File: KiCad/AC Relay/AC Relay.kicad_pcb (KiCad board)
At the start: 2 copper layers, 49.5 x 49.5 mm, 17 parts, among them J1 Screw_Terminal_01x02, J2 Conn_01x06_Female, J3 Screw_Terminal_01x02, K1 1461492-2, Q1 FDN537N, SW1 SW_Push, U1 BU33SD5WG-TR, U2 ESP-12E, U3 HLK-PM01

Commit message: title edited
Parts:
- added REF**: TerminalBlock_RND_205-00045_1x02_P5.00mm_Horizontal, TerminalBlock_RND:TerminalBlock_RND_205-00045_1x02_P5.00mm_Horizontal, F.Cu at (59.7, 61.0)
- moved J3 0.82 mm to (75.3, 71.0)
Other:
- board text added: "BTBM_1 Rev.: 1 S/N:0001"
- board text added: "DANGER KEEP OUT HIGH VOLTAGE AREA"
- board text added: "Relay 10A"
- board text removed: "AC Relay - ESP8266 Design by Enrique Gómez CC BY-SA 4.0 enriquegomez.me Rev.: 4 - S/N:"
- board text removed: "DANGER HIGH VOLTAGE AREA"
- board text removed: "Relay Max. 16 A"

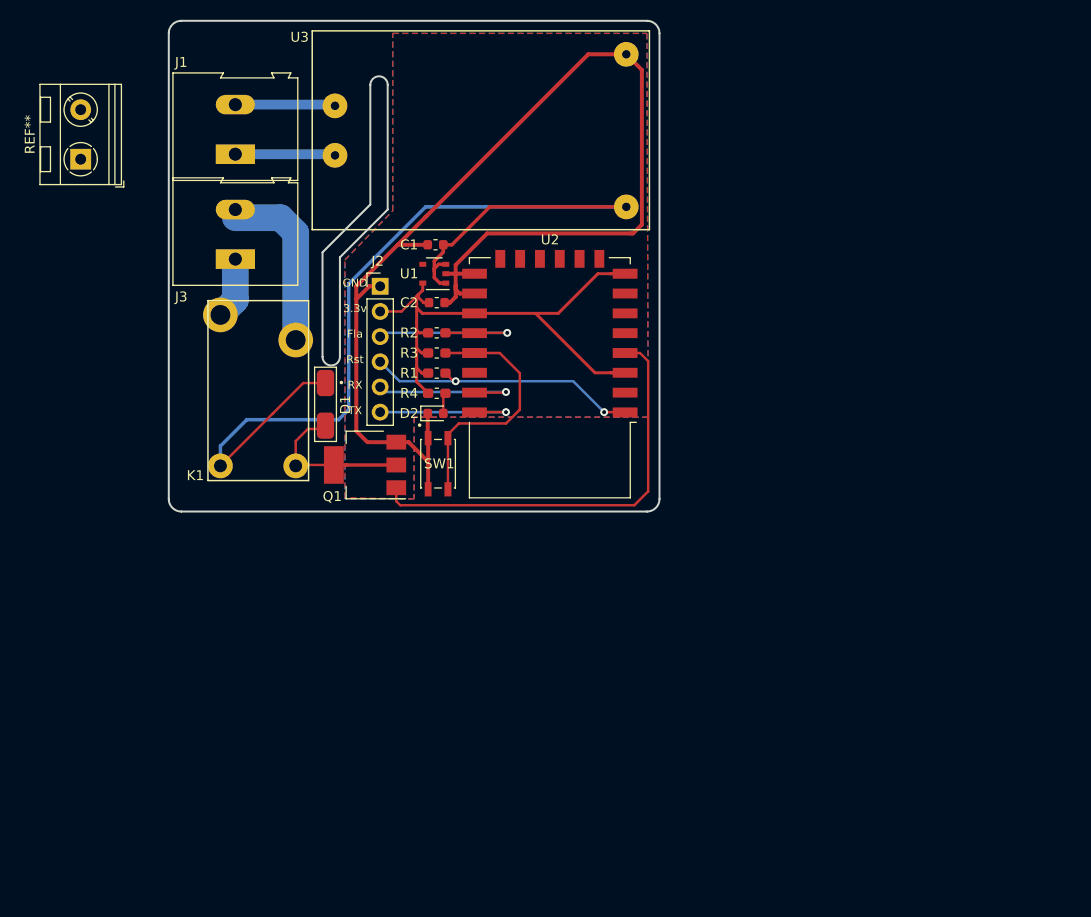
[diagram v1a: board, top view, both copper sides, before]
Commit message: until components placemaent
done all until com placement, but had isssue in edge cut .
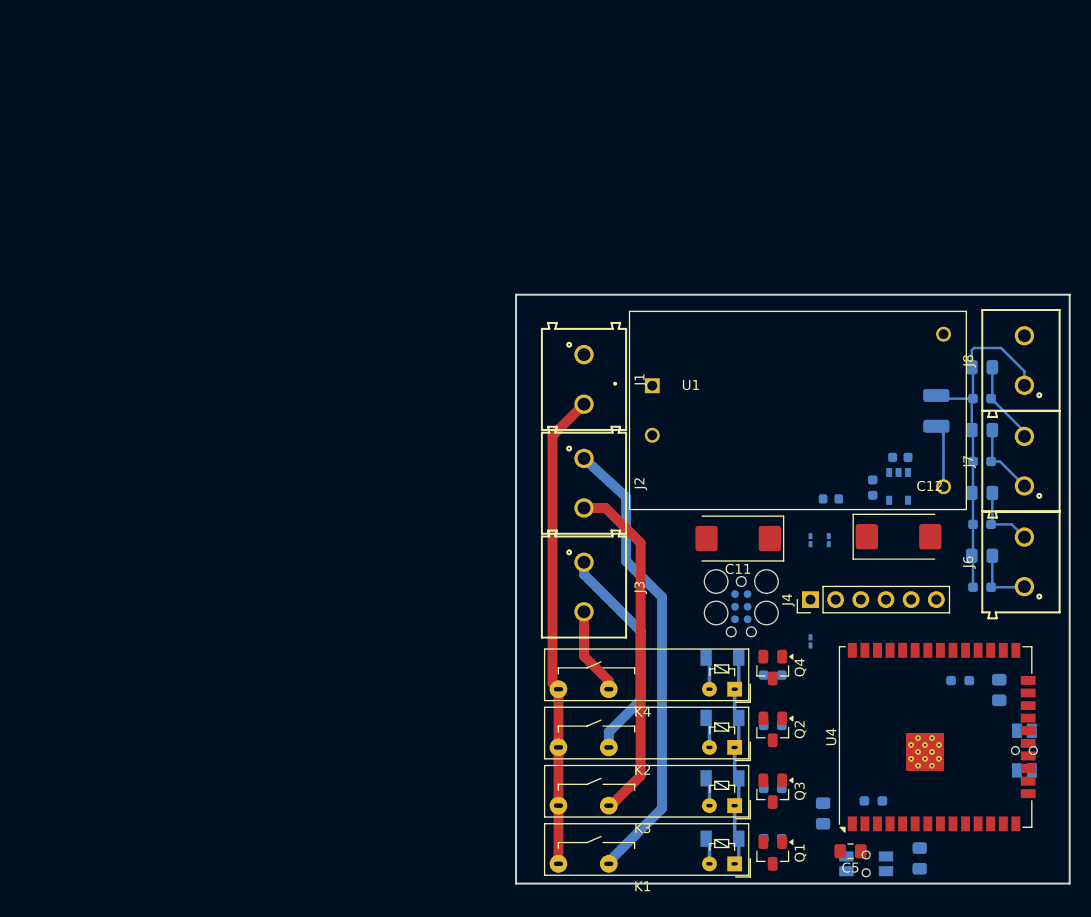
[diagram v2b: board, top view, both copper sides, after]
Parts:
- removed R1, R2, R3: 10k, Resistor_SMD:R_0603_1608Metric_Pad1.05x0.95mm_HandSolder
- removed R4: 82.5, Resistor_SMD:R_0603_1608Metric_Pad1.05x0.95mm_HandSolder
- removed REF**: TerminalBlock_RND_205-00045_1x02_P5.00mm_Horizontal, TerminalBlock_RND:TerminalBlock_RND_205-00045_1x02_P5.00mm_Horizontal
- removed SW1: SW_Push, Button_Switch_SMD:SW_SPST_EVQP2
- removed U3: HLK-PM01, red:HLK-PM01
- added C10: 0.1uf, Capacitor_SMD:C_0805_2012Metric_Pad1.18x1.45mm_HandSolder, B.Cu at (150.7, 88.3)
- added C11: 100uF T cap, Capacitor_Tantalum_SMD:CP_EIA-7343-20_Kemet-V_Pad2.25x2.55mm_HandSolder, F.Cu at (126.1, 99.2)
- added C12: 100uF T cap, Capacitor_Tantalum_SMD:CP_EIA-7343-20_Kemet-V_Pad2.25x2.55mm_HandSolder, F.Cu at (142.2, 99.1)
- added C3: 0.1uf, Capacitor_SMD:C_0805_2012Metric_Pad1.18x1.45mm_HandSolder, B.Cu at (144.4, 131.5)
- added C4: 10uf, Capacitor_SMD:C_0805_2012Metric_Pad1.18x1.45mm_HandSolder, B.Cu at (134.6, 127.0)
- added C5: 0.1uf, Capacitor_SMD:C_0805_2012Metric_Pad1.18x1.45mm_HandSolder, F.Cu at (137.4, 130.8)
- added C6: 0.1uf, Capacitor_SMD:C_0805_2012Metric_Pad1.18x1.45mm_HandSolder, B.Cu at (152.4, 114.5)
- added C7: 0.1uf, Capacitor_SMD:C_0805_2012Metric_Pad1.18x1.45mm_HandSolder, B.Cu at (150.7, 94.6)
- added C8: 0.1uf, Capacitor_SMD:C_0805_2012Metric_Pad1.18x1.45mm_HandSolder, B.Cu at (150.7, 101.0)
- added C9: 0.1uf, Capacitor_SMD:C_0805_2012Metric_Pad1.18x1.45mm_HandSolder, B.Cu at (150.7, 82.0)
- added D3: LL4148, Rak_FP_Library:LL4148, B.Cu at (124.5, 117.3)
- added D4: LL4148, Rak_FP_Library:LL4148, B.Cu at (124.5, 123.4)
- added D5: LL4148, Rak_FP_Library:LL4148, B.Cu at (124.5, 111.3)
- added J4: Conn_01x06_Female, Connector_PinHeader_2.54mm:PinHeader_1x06_P2.54mm_Vertical, F.Cu at (133.3, 105.4)
- added J6: TB002-500-02BE, Rak_FP_Library:2_terminal_block_small, F.Cu at (154.9, 101.6)
- added J7: TB002-500-02BE, Rak_FP_Library:2_terminal_block_small, F.Cu at (154.9, 91.4)
- added J8: TB002-500-02BE, Rak_FP_Library:2_terminal_block_small, F.Cu at (154.9, 81.3)
- added J9: Conn_ARM_SWD_TagConnect_TC2030, Connector:Tag-Connect_TC2030-IDC-FP_2x03_P1.27mm_Vertical, B.Cu at (126.4, 106.1)
- added K2: 1-2071556-1, Rak_FP_Library:Relay_SPST_Fanahar_5A, F.Cu at (125.7, 120.3)
- added K3: 1-2071556-1, Rak_FP_Library:Relay_SPST_Fanahar_5A, F.Cu at (125.7, 126.2)
- added K4: 1-2071556-1, Rak_FP_Library:Relay_SPST_Fanahar_5A, F.Cu at (125.7, 114.5)
- added Q2: FDN537N, Package_TO_SOT_SMD:SuperSOT-3, F.Cu at (129.5, 118.5)
- added Q3: FDN537N, Package_TO_SOT_SMD:SuperSOT-3, F.Cu at (129.5, 124.7)
- added Q4: FDN537N, Package_TO_SOT_SMD:SuperSOT-3, F.Cu at (129.5, 112.3)
- added R10: 10K, Resistor_SMD:R_0603_1608Metric_Pad0.98x0.95mm_HandSolder, B.Cu at (150.7, 91.5)
- added R11: 330R, Resistor_SMD:R_1210_3225Metric_Pad1.30x2.65mm_HandSolder, B.Cu at (146.1, 86.4)
- added R12: 1K, Resistor_SMD:R_0603_1608Metric_Pad0.98x0.95mm_HandSolder, B.Cu at (129.5, 129.5)
- added R13: 0R, Resistor_SMD:R_0201_0603Metric_Pad0.64x0.40mm_HandSolder, B.Cu at (133.3, 109.6)
- added R14: 0R, Resistor_SMD:R_0201_0603Metric_Pad0.64x0.40mm_HandSolder, B.Cu at (133.3, 99.4)
- added R15: NA, Resistor_SMD:R_0201_0603Metric_Pad0.64x0.40mm_HandSolder, B.Cu at (135.2, 99.4)
- added R16: 1K, Resistor_SMD:R_0603_1608Metric_Pad0.98x0.95mm_HandSolder, B.Cu at (129.5, 113.0)
- added R17: 1K, Resistor_SMD:R_0603_1608Metric_Pad0.98x0.95mm_HandSolder, B.Cu at (129.5, 124.5)
- added R18: 1K, Resistor_SMD:R_0603_1608Metric_Pad0.98x0.95mm_HandSolder, B.Cu at (129.5, 118.1)
- added R5: 10K, Resistor_SMD:R_0603_1608Metric_Pad0.98x0.95mm_HandSolder, B.Cu at (148.5, 113.6)
- added R6: 12K, Resistor_SMD:R_0603_1608Metric_Pad0.98x0.95mm_HandSolder, B.Cu at (139.7, 125.7)
- added R7: 10K, Resistor_SMD:R_0603_1608Metric_Pad0.98x0.95mm_HandSolder, B.Cu at (150.7, 97.8)
- added R8: 10K, Resistor_SMD:R_0603_1608Metric_Pad0.98x0.95mm_HandSolder, B.Cu at (150.7, 104.2)
- added R9: 10K, Resistor_SMD:R_0603_1608Metric_Pad0.98x0.95mm_HandSolder, B.Cu at (150.7, 85.1)
- added SW2: Boot, Rak_FP_Library:SW_SPST_withpost, B.Cu at (154.9, 120.7)
- added SW3: Rst, Rak_FP_Library:SW_SPST_withpost, B.Cu at (139.0, 132.1)
- added U4: ESP32-WROOM-32UE, Rak_FP_Library:ESP32-WROOM-32UE, F.Cu at (146.0, 119.3)
- C1, C2: value 0.47uF -> 1uF; moved to B.Cu
- D1: value RGF1B -> LED_verde; footprint Diode_SMD:D_0603_1608Metric -> LED_SMD:LED_0603_1608Metric; moved to B.Cu
- D2: value LED_verde -> LL4148; footprint LED_SMD:LED_0603_1608Metric -> Rak_FP_Library:LL4148; moved to B.Cu
- J1, J3: footprint TerminalBlock:TerminalBlock_Altech_AK300-2_P5.00mm -> Rak_FP_Library:2_terminal_block
- J2: value Conn_01x06_Female -> Screw_Terminal_01x02; footprint Connector_PinHeader_2.54mm:PinHeader_1x06_P2.54mm_Vertical -> Rak_FP_Library:2_terminal_block
- K1: value 1461492-2 -> 1-2071556-1; footprint red:Rele-1461492-2 -> Rak_FP_Library:Relay_SPST_Fanahar_5A
- Q1: footprint Package_TO_SOT_SMD:SOT-223 -> Package_TO_SOT_SMD:SuperSOT-3
- U1: value BU33SD5WG-TR -> HLK-PM01; footprint Package_SO:TSOP-5_1.65x3.05mm_P0.95mm -> Rak_FP_Library:CONV_HLK-PM01
- U2: value ESP-12E -> BU33SD5WG-TR; footprint RF_Module:ESP-12E -> Rak_FP_Library:SOT95P280X125-5N; moved to B.Cu
- moved K1 57.8 mm to (125.7, 132.1), turned to 180 degrees
- moved Q1 56.8 mm to (129.5, 131.0), turned to -90 degrees
- moved D2 51.8 mm to (124.5, 129.5), turned to 180 degrees
- moved C1 51.6 mm to (142.4, 91.1)
- moved D1 51.5 mm to (135.4, 95.2), turned to 180 degrees
- moved J3 48.3 mm to (110.5, 104.1), turned to -90 degrees
- moved C2 47.8 mm to (139.6, 94.1), turned to 90 degrees
- moved J1 41.9 mm to (110.5, 83.2), turned to -90 degrees
- moved U1 39.2 mm to (132.1, 86.3), turned to 0 degrees
- moved U2 36.9 mm to (142.2, 94.0), turned to -90 degrees
- moved J2 28.6 mm to (110.5, 93.7), turned to -90 degrees
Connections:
- D1 pad 1: Net-(D1-Pad1) -> GND
- D1 pad 2: +5V -> Net-(D1-A)
- D2 pad 1: GND -> +5V
- D2 pad 2: Net-(D2-Pad2) -> Net-(D2-A)
- J1 pad 1: Net-(J1-Pad1) -> /AC to DC conv/Neutral
- J1 pad 2: Net-(J1-Pad2) -> /AC to DC conv/Phase
- J2 pad 1: GND -> Net-(J2-Pin_1)
- J2 pad 2: +3V3 -> Net-(J2-Pin_2)
- J3 pad 1: Net-(J3-Pad1) -> Net-(J3-Pin_1)
- J3 pad 2: Net-(J3-Pad2) -> Net-(J3-Pin_2)
- Q1 pad 1: /Relay -> /Relay and diver/Rel_sig1
- Q1 pad 2: Net-(D1-Pad1) -> Net-(D2-A)
- U1 pad 1: +5V -> /AC to DC conv/Neutral
- U1 pad 2: GND -> /AC to DC conv/Phase
- U1 pad 3: +5V -> GND
- U1 pad 4: Net-(U1-Pad4) -> +5V
- U2 pad 1: /Rst -> +5V
- U2 pad 2: Net-(U2-Pad2) -> GND
- U2 pad 3: +3V3 -> +5V
- U2 pad 4: /Relay -> unconnected-(U2-N.C.-Pad4)
- U2 pad 5: Net-(U2-Pad5) -> +3V3
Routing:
- net GND: track 122.5 -> 0.00 mm
- net +5V: track 101.0 -> 28.5 mm
- net +3V3: track 58.2 -> 0.00 mm
- net /AC to DC conv/Phase: track 0.00 -> 48.0 mm
- net Net-(J2-Pin_1): track 0.00 -> 46.5 mm
- net /Relay: track 43.3 -> 0.00 mm
- net Net-(C10-Pad2): track 0.00 -> 35.9 mm
- net Net-(J2-Pin_2): track 0.00 -> 35.1 mm
- net /Rst: track 28.3 -> 0.00 mm, vias 2 -> 0
- net /Button: track 25.9 -> 0.00 mm
- net Net-(J3-Pin_1): track 0.00 -> 22.4 mm
- net /Flash: track 19.2 -> 0.00 mm, vias 1 -> 0
- net Net-(J3-Pad2): track 17.5 -> 0.00 mm
- net Net-(D1-Pad1): track 17.0 -> 0.00 mm
- net /RX: track 16.0 -> 0.00 mm, vias 1 -> 0
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- removed copper zone on B.Cu, net GND
- removed copper zone on F.Cu, net GND
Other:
- board size 49.5 x 49.5 mm -> 55.9 x 59.4 mm
- copper layers 2 -> 4
- board text removed: "AC in"
- board text removed: "BTBM_1 Rev.: 1 S/N:0001"
- board text removed: "DANGER KEEP OUT HIGH VOLTAGE AREA"
- board text removed: "GND 3.3v Fla Rst RX TX"
- board text removed: "Relay 10A"
